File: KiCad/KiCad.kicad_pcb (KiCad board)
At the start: 2 copper layers, 28 parts, among them J1 Conn_01x04_Male, J2 Conn_01x04_Male, J3 Conn_01x04_Male, J4 USB_B_Micro, SW1 SW_SPDT, U1 AMS1117-3.3, U2 STM32F103C8T6, Y1 Crystal_GND24

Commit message: Routed power supply components
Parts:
- moved C3 50.8 mm to (121.5, 81.6)
- moved C1 36.6 mm to (134.2, 92.6)
- moved C2 24.2 mm to (138.8, 96.8), turned to 90 degrees
- moved R1 17.1 mm to (141.6, 95.0), turned to 90 degrees
- moved U1 15.9 mm to (134.0, 98.2), turned to -90 degrees
- moved D1 14.1 mm to (141.5, 97.7), turned to -90 degrees
- moved J2 1.41 mm to (122.5, 101.1)
- moved J4 0.57 mm to (139.4, 88.0)
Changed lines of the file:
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@@
   )
   (footprint "Package_TO_SOT_SMD:SOT-223-3_TabPin2" (layer "F.Cu")
-    (at 146.31 108.21)
+    (at 134 98.15 -90)
     (descr "module CMS SOT223 4 pins")
     (tags "CMS SOT")
@@
     (property "Sheetname" "")
     (attr smd)
-    (fp_text reference "U1" (at 0 -4.5) (layer "F.SilkS")
-      (effects (font (size 1 1) (thickness 0.15)))
-    )
-    (fp_text value "AMS1117-3.3" (at 0 4.5) (layer "F.Fab")
-      (effects (font (size 1 1) (thickness 0.15)))
-    )
-    (fp_text user "${REFERENCE}" (at 0 0 90) (layer "F.Fab")
+    (fp_text reference "U1" (at 5.3 -3.2 180) (layer "F.SilkS")
+      (effects (font (size 1 1) (thickness 0.15)))
+    )
+    (fp_text value "AMS1117-3.3" (at 0 4.5 90) (layer "F.Fab")
+      (effects (font (size 1 1) (thickness 0.15)))
+    )
+    (fp_text user "${REFERENCE}" (at 0 0) (layer "F.Fab")
       (effects (font (size 0.8 0.8) (thickness 0.12)))
     )
@@
     (fp_line (start -1.85 3.35) (end 1.85 3.35) (layer "F.Fab") (width 0.1))
     (fp_line (start 1.85 -3.35) (end 1.85 3.35) (layer "F.Fab") (width 0.1))
-    (pad "1" smd rect (at -3.15 -2.3) (size 2 1.5) (layers "F.Cu" "F.Paste" "F.Mask")
+    (pad "1" smd rect (at -3.15 -2.3 270) (size 2 1.5) (layers "F.Cu" "F.Paste" "F.Mask")
       (net 2 "GND") (pinfunction "GND") (pintype "power_in"))
-    (pad "2" smd rect (at -3.15 0) (size 2 1.5) (layers "F.Cu" "F.Paste" "F.Mask")
+    (pad "2" smd rect (at -3.15 0 270) (size 2 1.5) (layers "F.Cu" "F.Paste" "F.Mask")
       (net 3 "+3.3V") (pinfunction "VO") (pintype "power_out"))
-    (pad "2" smd rect (at 3.15 0) (size 2 3.8) (layers "F.Cu" "F.Paste" "F.Mask")
+    (pad "2" smd rect (at 3.15 0 270) (size 2 3.8) (layers "F.Cu" "F.Paste" "F.Mask")
       (net 3 "+3.3V") (pinfunction "VO") (pintype "power_out"))
-    (pad "3" smd rect (at -3.15 2.3) (size 2 1.5) (layers "F.Cu" "F.Paste" "F.Mask")
+    (pad "3" smd rect (at -3.15 2.3 270) (size 2 1.5) (layers "F.Cu" "F.Paste" "F.Mask")
       (net 1 "VBUS") (pinfunction "VI") (pintype "power_in"))
     (model "${KICAD6_3DMODEL_DIR}/Package_TO_SOT_SMD.3dshapes/SOT-223.wrl"
@@
   )
   (footprint "Capacitor_SMD:C_0603_1608Metric" (layer "F.Cu")
-    (at 159.89 114.808)
+    (at 121.45 81.6)
     (descr "Capacitor SMD 0603 (1608 Metric), square (rectangular) end terminal, IPC_7351 nominal, (Body size source: IPC-SM-782 page 76, https://www.pcb-3d.com/wordpress/wp-content/uploads/ipc-sm-782a_amendment_1_and_2.pdf), generated with kicad-footprint-generator")
     (tags "capacitor")
@@
   )
   (footprint "Connector_USB:USB_Micro-B_Wuerth_629105150521" (layer "F.Cu")
-    (at 139.518 88.561 90)
+    (at 139.4 88 90)
     (descr "USB Micro-B receptacle, http://www.mouser.com/ds/2/445/629105150521-469306.pdf")
     (tags "usb micro receptacle")
@@
   )
   (footprint "Capacitor_SMD:C_0805_2012Metric" (layer "F.Cu")
-    (at 160.11 108.3)
+    (at 138.8 96.8 90)
     (descr "Capacitor SMD 0805 (2012 Metric), square (rectangular) end terminal, IPC_7351 nominal, (Body size source: IPC-SM-782 page 76, https://www.pcb-3d.com/wordpress/wp-content/uploads/ipc-sm-782a_amendment_1_and_2.pdf, https://docs.google.com/spreadsheets/d/1BsfQQcO9C6DZCsRaXUlFlo91Tg2WpOkGARC1WS5S8t0/edit?usp=sharing), generated with kicad-footprint-generator")
     (tags "capacitor")
@@
     (property "Sheetname" "")
     (attr smd)
-    (fp_text reference "C2" (at 0 -1.68) (layer "F.SilkS")
-      (effects (font (size 1 1) (thickness 0.15)))
-    )
-    (fp_text value "22u" (at 0 1.68) (layer "F.Fab")
-      (effects (font (size 1 1) (thickness 0.15)))
-    )
-    (fp_text user "${REFERENCE}" (at 0 0) (layer "F.Fab")
+    (fp_text reference "C2" (at 2.4 0.2 180) (layer "F.SilkS")
+      (effects (font (size 1 1) (thickness 0.15)))
+    )
+    (fp_text value "22u" (at 0 1.68 90) (layer "F.Fab")
+      (effects (font (size 1 1) (thickness 0.15)))
+    )
+    (fp_text user "${REFERENCE}" (at 0 0 90) (layer "F.Fab")
       (effects (font (size 0.5 0.5) (thickness 0.08)))
     )
@@
     (fp_line (start 1 -0.625) (end 1 0.625) (layer "F.Fab") (width 0.1))
     (fp_line (start -1 -0.625) (end 1 -0.625) (layer "F.Fab") (width 0.1))
-    (pad "1" smd roundrect (at -0.95 0) (size 1 1.45) (layers "F.Cu" "F.Paste" "F.Mask") (roundrect_rratio 0.25)
+    (pad "1" smd roundrect (at -0.95 0 90) (size 1 1.45) (layers "F.Cu" "F.Paste" "F.Mask") (roundrect_rratio 0.25)
       (net 3 "+3.3V") (pintype "passive"))
-    (pad "2" smd roundrect (at 0.95 0) (size 1 1.45) (layers "F.Cu" "F.Paste" "F.Mask") (roundrect_rratio 0.25)
+    (pad "2" smd roundrect (at 0.95 0 90) (size 1 1.45) (layers "F.Cu" "F.Paste" "F.Mask") (roundrect_rratio 0.25)
       (net 2 "GND") (pintype "passive"))
     (model "${KICAD6_3DMODEL_DIR}/Capacitor_SMD.3dshapes/C_0805_2012Metric.wrl"
@@
   )
   (footprint "LED_SMD:LED_0603_1608Metric" (layer "F.Cu")
-    (at 153.28 105.38)
+    (at 141.5 97.65 -90)
     (descr "LED SMD 0603 (1608 Metric), square (rectangular) end terminal, IPC_7351 nominal, (Body size source: http://www.tortai-tech.com/upload/download/2011102023233369053.pdf), generated with kicad-footprint-generator")
     (tags "LED")
@@
     (property "Sheetname" "")
     (attr smd)
-    (fp_text reference "D1" (at 0 -1.43) (layer "F.SilkS")
-      (effects (font (size 1 1) (thickness 0.15)))
-    )
-    (fp_text value "RED" (at 0 1.43) (layer "F.Fab")
-      (effects (font (size 1 1) (thickness 0.15)))
-    )
-    (fp_text user "${REFERENCE}" (at 0 0) (layer "F.Fab")
+    (fp_text reference "D1" (at 0.6 -1.9 180) (layer "F.SilkS")
+      (effects (font (size 1 1) (thickness 0.15)))
+    )
+    (fp_text value "RED" (at 0 1.43 90) (layer "F.Fab")
+      (effects (font (size 1 1) (thickness 0.15)))
+    )
+    (fp_text user "${REFERENCE}" (at 0 0 90) (layer "F.Fab")
       (effects (font (size 0.4 0.4) (thickness 0.06)))
     )
@@
     (fp_line (start -0.5 -0.4) (end -0.8 -0.1) (layer "F.Fab") (width 0.1))
     (fp_line (start 0.8 0.4) (end 0.8 -0.4) (layer "F.Fab") (width 0.1))
-    (pad "1" smd roundrect (at -0.7875 0) (size 0.875 0.95) (layers "F.Cu" "F.Paste" "F.Mask") (roundrect_rratio 0.25)
+    (pad "1" smd roundrect (at -0.7875 0 270) (size 0.875 0.95) (layers "F.Cu" "F.Paste" "F.Mask") (roundrect_rratio 0.25)
       (net 8 "/Power_LED") (pinfunction "K") (pintype "passive"))
-    (pad "2" smd roundrect (at 0.7875 0) (size 0.875 0.95) (layers "F.Cu" "F.Paste" "F.Mask") (roundrect_rratio 0.25)
+    (pad "2" smd roundrect (at 0.7875 0 270) (size 0.875 0.95) (layers "F.Cu" "F.Paste" "F.Mask") (roundrect_rratio 0.25)
       (net 3 "+3.3V") (pinfunction "A") (pintype "passive"))
     (model "${KICAD6_3DMODEL_DIR}/LED_SMD.3dshapes/LED_0603_1608Metric.wrl"
@@
   )
   (footprint "Resistor_SMD:R_0402_1005Metric" (layer "F.Cu")
-    (at 158.6 95.6)
+    (at 141.55 95.04 90)
     (descr "Resistor SMD 0402 (1005 Metric), square (rectangular) end terminal, IPC_7351 nominal, (Body size source: IPC-SM-782 page 72, https://www.pcb-3d.com/wordpress/wp-content/uploads/ipc-sm-782a_amendment_1_and_2.pdf), generated with kicad-footprint-generator")
     (tags "resistor")
@@
     (property "Sheetname" "")
     (attr smd)
-    (fp_text reference "R1" (at 0 -1.17) (layer "F.SilkS")
-      (effects (font (size 1 1) (thickness 0.15)))
-    )
-    (fp_text value "1k5" (at 0 1.17) (layer "F.Fab")
-      (effects (font (size 1 1) (thickness 0.15)))
-    )
-    (fp_text user "${REFERENCE}" (at 0 0) (layer "F.Fab")
+    (fp_text reference "R1" (at 0.11 1.75 180) (layer "F.SilkS")
+      (effects (font (size 1 1) (thickness 0.15)))
+    )
+    (fp_text value "1k5" (at 0 1.17 90) (layer "F.Fab")
+      (effects (font (size 1 1) (thickness 0.15)))
+    )
+    (fp_text user "${REFERENCE}" (at 0 0 90) (layer "F.Fab")
       (effects (font (size 0.26 0.26) (thickness 0.04)))
     )
@@
     (fp_line (start 0.525 -0.27) (end 0.525 0.27) (layer "F.Fab") (width 0.1))
     (fp_line (start -0.525 -0.27) (end 0.525 -0.27) (layer "F.Fab") (width 0.1))
-    (pad "1" smd roundrect (at -0.51 0) (size 0.54 0.64) (layers "F.Cu" "F.Paste" "F.Mask") (roundrect_rratio 0.25)
+    (pad "1" smd roundrect (at -0.51 0 90) (size 0.54 0.64) (layers "F.Cu" "F.Paste" "F.Mask") (roundrect_rratio 0.25)
       (net 8 "/Power_LED") (pintype "passive"))
-    (pad "2" smd roundrect (at 0.51 0) (size 0.54 0.64) (layers "F.Cu" "F.Paste" "F.Mask") (roundrect_rratio 0.25)
+    (pad "2" smd roundrect (at 0.51 0 90) (size 0.54 0.64) (layers "F.Cu" "F.Paste" "F.Mask") (roundrect_rratio 0.25)
       (net 2 "GND") (pintype "passive"))
     (model "${KICAD6_3DMODEL_DIR}/Resistor_SMD.3dshapes/R_0402_1005Metric.wrl"
@@
   )
   (footprint "Capacitor_SMD:C_0805_2012Metric" (layer "F.Cu")
-    (at 170.18 99.06)
+    (at 134.15 92.6)
     (descr "Capacitor SMD 0805 (2012 Metric), square (rectangular) end terminal, IPC_7351 nominal, (Body size source: IPC-SM-782 page 76, https://www.pcb-3d.com/wordpress/wp-content/uploads/ipc-sm-782a_amendment_1_and_2.pdf, https://docs.google.com/spreadsheets/d/1BsfQQcO9C6DZCsRaXUlFlo91Tg2WpOkGARC1WS5S8t0/edit?usp=sharing), generated with kicad-footprint-generator")
     (tags "capacitor")
@@
   )
   (footprint "Connector_PinHeader_2.00mm:PinHeader_1x04_P2.00mm_Vertical" (layer "F.Cu")
-    (at 122.349 99.695 90)
+    (at 122.5 101.1 90)
     (descr "Through hole straight pin header, 1x04, 2.00mm pitch, single row")
     (tags "Through hole pin header THT 1x04 2.00mm single row")

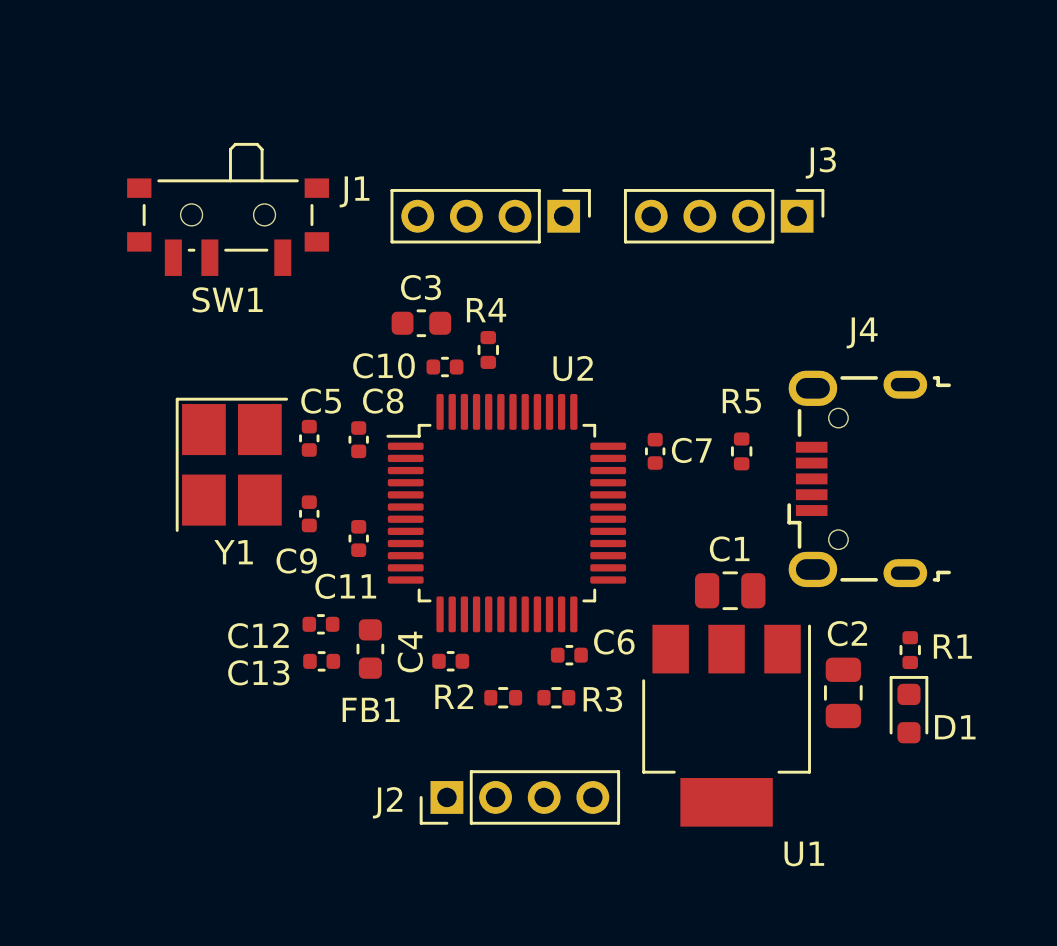
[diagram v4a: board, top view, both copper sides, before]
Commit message: Added Mounting holes and arranged board outline
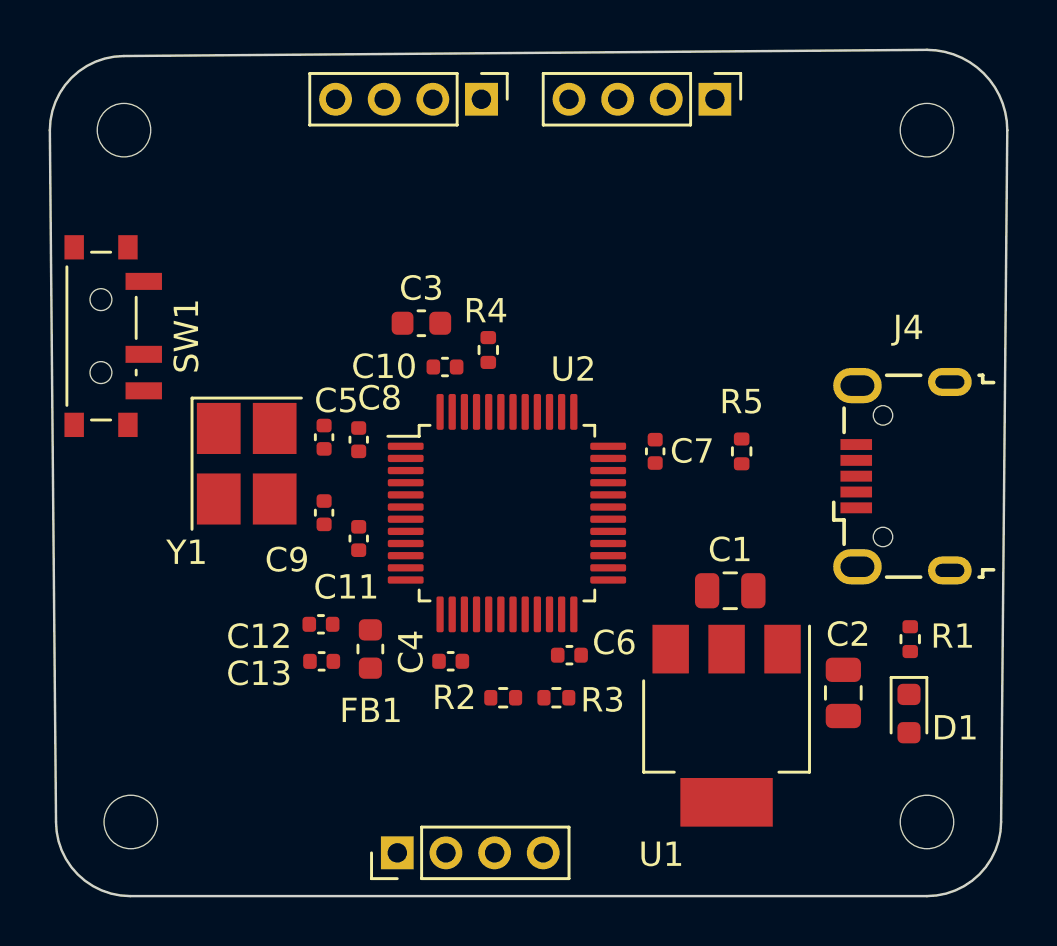
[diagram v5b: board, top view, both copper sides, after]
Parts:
- added H1: MountingHole, MountingHole:MountingHole_2.2mm_M2, F.Cu at (109.5, 102.1)
- added H2: MountingHole, MountingHole:MountingHole_2.2mm_M2, F.Cu at (142.2, 73.7)
- added H3: MountingHole, MountingHole:MountingHole_2.2mm_M2, F.Cu at (109.2, 73.7)
- added H4: MountingHole, MountingHole:MountingHole_2.2mm_M2, F.Cu at (142.2, 102.1)
- moved SW1 6.76 mm to (108.6, 82.1), turned to -90 degrees
- moved J1 5.88 mm to (123.9, 72.4)
- moved J3 5.88 mm to (133.5, 72.4)
- moved J2 3.06 mm to (120.5, 103.4)
- moved J4 1.83 mm to (141.2, 87.9)
- moved C9 0.61 mm to (117.4, 89.4)
- moved C5 0.61 mm to (117.4, 86.3)
- moved Y1 0.61 mm to (114.3, 87.4)
- moved R1 0.45 mm to (141.6, 94.6)
- turned C8 to 90 degrees
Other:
- board outline added: 39.4 x 34.8 mm
